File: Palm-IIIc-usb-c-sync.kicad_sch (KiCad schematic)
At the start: 28 parts, among them J1 USB_C_Receptacle_USB2.0, J2 Conn_01x05, J3 Conn_01x05, U1 CP2102N-Axx-xQFN20, U2 TRSF3232E

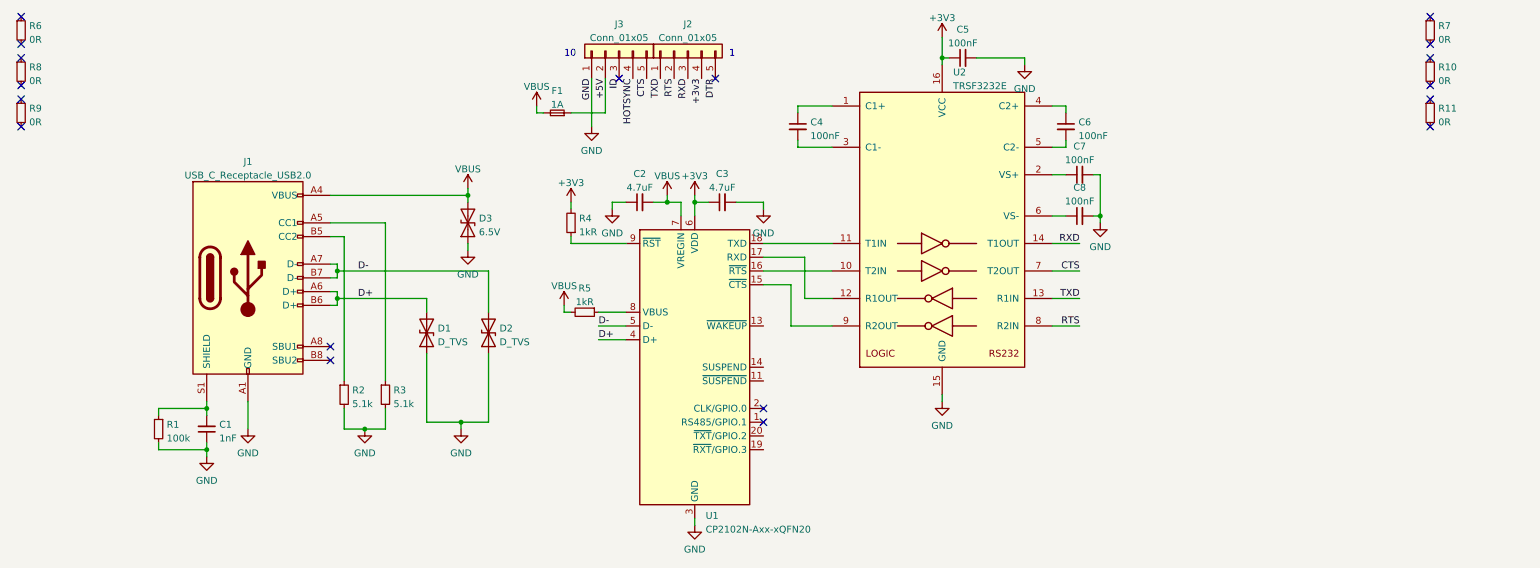
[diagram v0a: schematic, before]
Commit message: Add manufacturing markings
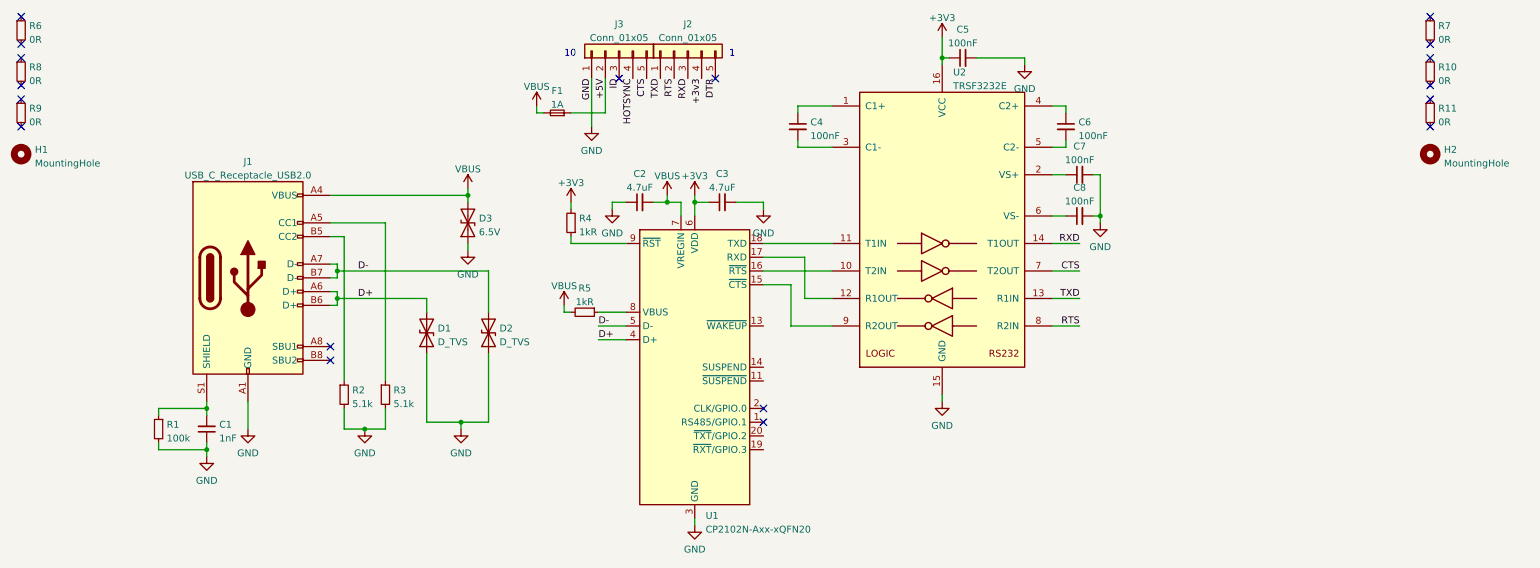
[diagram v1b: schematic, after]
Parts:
- added H1, H2: MountingHole, ToolingHole:ToolingHole_JLCSMT, symbol Mechanical:MountingHole
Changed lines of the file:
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@@
     (pin "2")
+  )
+  (symbol (lib_id "Mechanical:MountingHole") (at 278.13 43.18 0) (unit 1)
+    (in_bom no) (on_board yes) (fields_autoplaced)
+    (property "Reference" "H2" (id 0) (at 280.67 42.3453 0)
+      (effects (font (size 1.27 1.27)) (justify left))
+    )
+    (property "Value" "MountingHole" (id 1) (at 280.67 44.8822 0)
+      (effects (font (size 1.27 1.27)) (justify left))
+    )
+    (property "Footprint" "ToolingHole:ToolingHole_JLCSMT" (id 2) (at 278.13 43.18 0)
+      (effects (font (size 1.27 1.27)) hide)
+    )
+    (property "Datasheet" "~" (id 3) (at 278.13 43.18 0)
+      (effects (font (size 1.27 1.27)) hide)
+    )
   )
   (symbol (lib_id "power:GND") (at 59.69 93.98 0) (unit 1)
@@
     (pin "1")
     (pin "2")
+  )
+  (symbol (lib_id "Mechanical:MountingHole") (at 17.78 43.18 0) (unit 1)
+    (in_bom no) (on_board yes) (fields_autoplaced)
+    (property "Reference" "H1" (id 0) (at 20.32 42.3453 0)
+      (effects (font (size 1.27 1.27)) (justify left))
+    )
+    (property "Value" "MountingHole" (id 1) (at 20.32 44.8822 0)
+      (effects (font (size 1.27 1.27)) (justify left))
+    )
+    (property "Footprint" "ToolingHole:ToolingHole_JLCSMT" (id 2) (at 17.78 43.18 0)
+      (effects (font (size 1.27 1.27)) hide)
+    )
+    (property "Datasheet" "~" (id 3) (at 17.78 43.18 0)
+      (effects (font (size 1.27 1.27)) hide)
+    )
   )
   (symbol (lib_id "power:VBUS") (at 118.11 71.12 0) (unit 1)
@@
       (reference "F1") (unit 1) (value "1A") (footprint "Fuse:Fuse_0402_1005Metric")
     )
+    (path "/bf52073c-3f45-4543-b505-7d69498b432f"
+      (reference "H1") (unit 1) (value "MountingHole") (footprint "ToolingHole:ToolingHole_JLCSMT")
+    )
+    (path "/45a36fc9-4ce5-4d10-8f5f-3d23bc3b3330"
+      (reference "H2") (unit 1) (value "MountingHole") (footprint "ToolingHole:ToolingHole_JLCSMT")
+    )
     (path "/1a47a2c5-f1fc-4236-80e4-40560355a7e1"
